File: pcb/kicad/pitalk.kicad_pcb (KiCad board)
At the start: 4 copper layers, 76 x 58 mm, 12 parts, among them J1 RPi_Zero2W, J2 WS_2in_Touch, J3 MAX98357A, J4 INMP441_A, J5 INMP441_B, J6 PB_LED

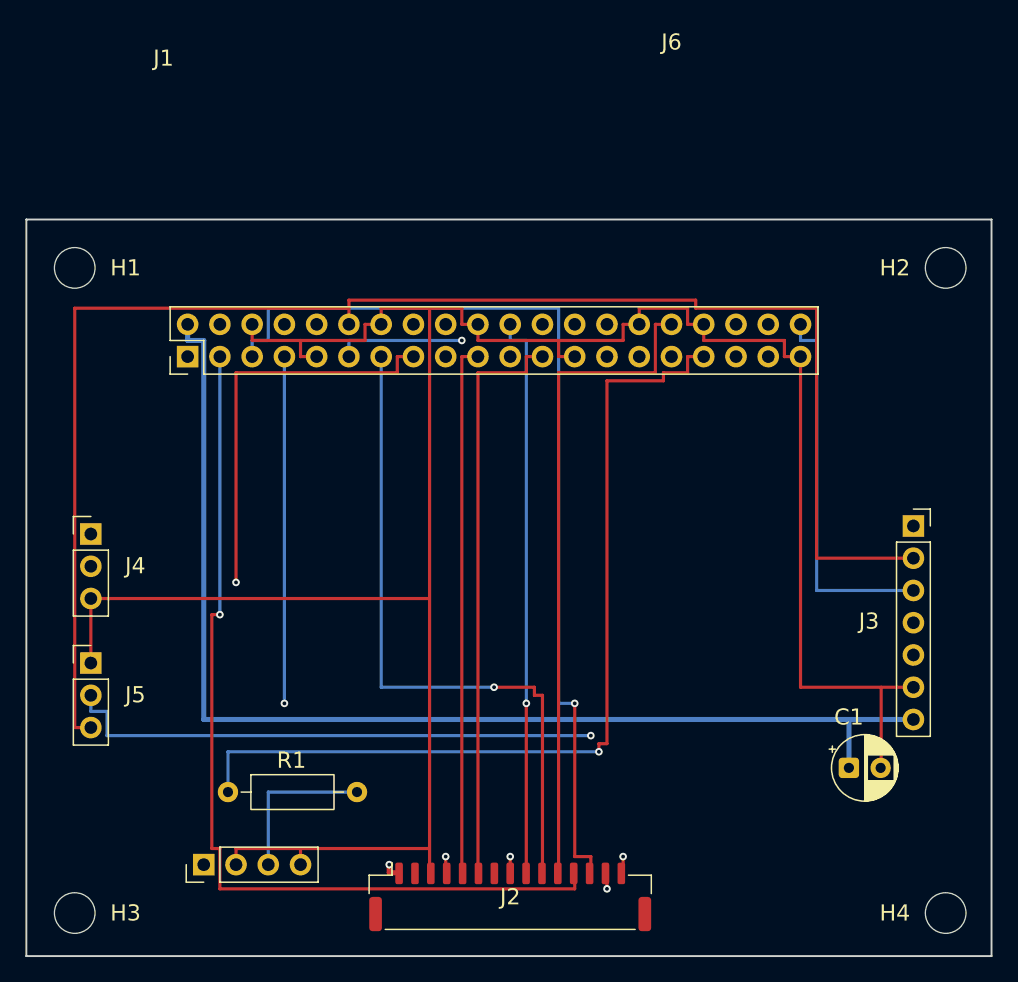
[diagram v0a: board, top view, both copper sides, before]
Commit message: Add connector pin labels to PCB silkscreen
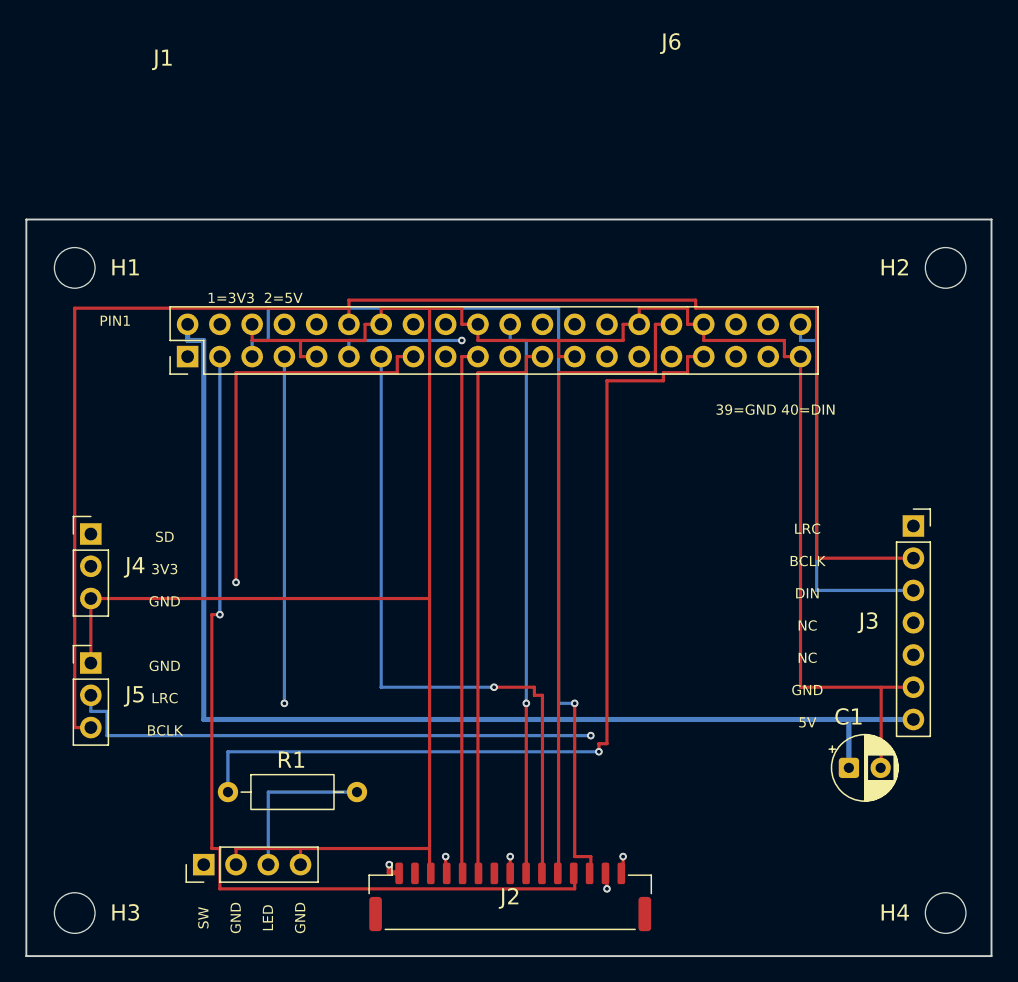
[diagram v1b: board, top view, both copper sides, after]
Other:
- board text added: "1=3V3 2=5V"
- board text added: "39=GND 40=DIN"
- board text added: "3V3"
- board text added: "5V"
- board text added: "BCLK"
- board text added: "DIN"
- board text added: "GND"
- board text added: "LED"
- board text added: "LRC"
- board text added: "NC"
- board text added: "PIN1"
- board text added: "SD"
- board text added: "SW"
